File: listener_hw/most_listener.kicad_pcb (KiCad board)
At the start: 2 copper layers, 130 x 90 mm, 125 parts, among them J1 1-1394640-1, J2 ANALYSER, J3 I2S, J4 VBAT_IN, J5 PLR135/T10, J6 PLT133/T10W, J7 RCA 75R, M1 Tang Nano 20K, M2 ESP32-DevKitC-VIE, U1 74LVC1G34, U10 TPS2553DBVR, U11 74LVC1G123, U12 DIR9001, U13 SRC4192, U14 LP5907MFX-3.3, U2 74LVC1G157, U3 74LVC1G125, U4 74LVC1G123, U5 TPS7B8133DRV, U6 LMR38020F, U7 Si514, U8 LP5907MFX-3.3, U9 74LVC1G79, X1 24.576MHz

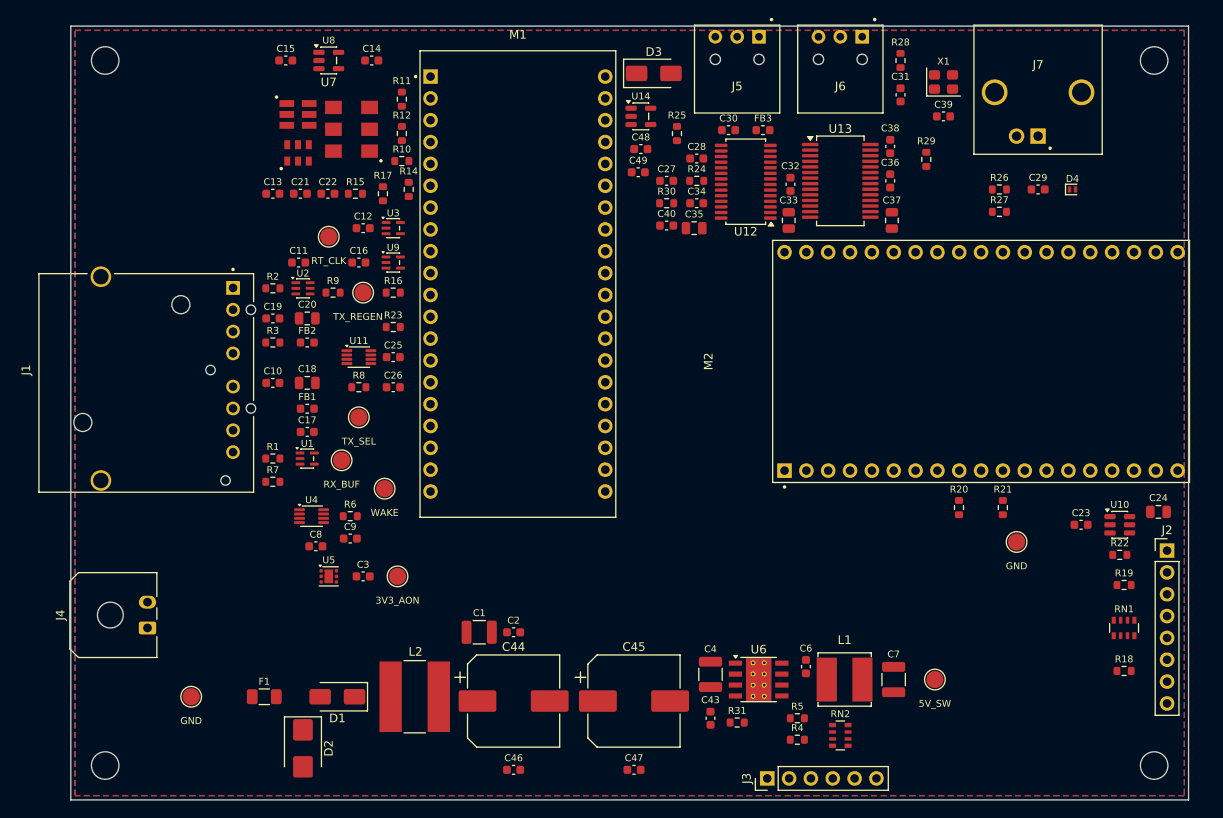
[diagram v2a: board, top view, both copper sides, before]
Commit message: Board: block 11, analog line out - PCM5102A on J3's stereo into the two RCA jacks placed by hand; footprints linked to the sheet
Sheet, block 11: U15 PCM5102A in hardware mode (FMT, FLT, DEMP low: I2S,
normal latency, no de-emphasis), SCK grounded so its PLL takes the clock from
BCK - three wires, the same I2S_BCLK_F / I2S_LRCK_F / I2S_DOUT_F that feed
J3 (64 Fs, 32-bit slots). XSMT from LOCK: muted while the ring is not locked
and while the FPGA is unconfigured (R8 holds LOCK low), with the chip's
104-sample soft ramp; no new FPGA pin, no gateware change. Outputs 2.1 Vrms
ground-centred through 470R + 2n2 C0G (TI SLAS859C Figure 33) to J8 (L) and
J9 (R), a PESD5V0S1BL at each jack as D4 at J7. U16, an LP5907, makes
3V3_DAC from 5V_SW; its output capacitance must stay within 10 uF (LP5907
data sheet), so AVDD gets 4.7 uF and CPVDD 2.2 uF instead of Figure 33's
10 uF each; LDOO 100n + 10u, flying cap and VNEG 2u2 each. Test points are
out of the BOM now (their footprints already said so). ERC clean.

Board: the placement the user reworked by hand since cddadba (the power
corner, block 9, J2/J3/U10 moved to the bottom middle, a fifth mounting hole
H5 at the top, two RCA jacks on the right edge copied from J7). The copies
became J9 (upper, right channel) and J8 (lower, left); block 11 sits in the
corner beside them, U15 turned so its analog pins face the jacks and its
digital pins face the I2S coming down from M2's pins. Every footprint now
carries its symbol's path and library name and single pins their
unconnected nets, the holes are board-only - DRC with --schematic-parity
finds no difference, so Update PCB from Schematic works from here. The
antenna keep-out is squared with M2 again. DRC: no error; the warnings are
silk, most of it in the hand-moved areas.

gen_listener_pcb.py writes the same links and parks parts its table does
not know beside the board instead of stopping. check_all.py's board step
also fails on any difference from the sheet. KiCad's local histor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
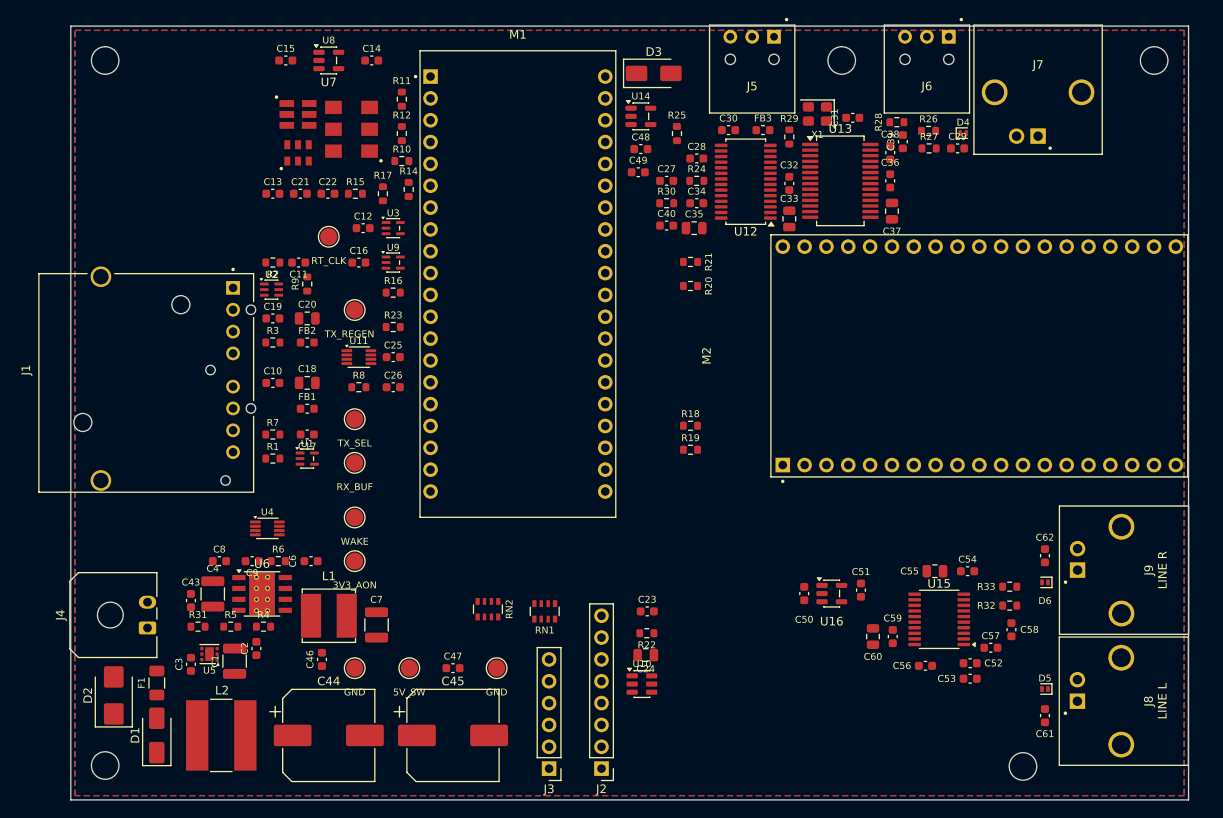
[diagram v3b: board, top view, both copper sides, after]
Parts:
- added C50: 1u, Capacitor_SMD:C_0603_1608Metric, F.Cu at (85.3, 66.0)
- added C51: 1u, Capacitor_SMD:C_0603_1608Metric, F.Cu at (91.9, 65.6)
- added C52: 100n, Capacitor_SMD:C_0603_1608Metric, F.Cu at (104.6, 74.1)
- added C53: 2u2, Capacitor_SMD:C_0603_1608Metric, F.Cu at (104.6, 75.9)
- added C54: 100n, Capacitor_SMD:C_0603_1608Metric, F.Cu at (104.3, 63.4)
- added C55: 4u7, Capacitor_SMD:C_0805_2012Metric, F.Cu at (100.5, 63.4)
- added C56: 100n, Capacitor_SMD:C_0603_1608Metric, F.Cu at (99.4, 74.4)
- added C57: 2u2, Capacitor_SMD:C_0603_1608Metric, F.Cu at (107.0, 72.3)
- added C58: 2u2, Capacitor_SMD:C_0603_1608Metric, F.Cu at (109.4, 70.2)
- added C59: 100n, Capacitor_SMD:C_0603_1608Metric, F.Cu at (95.6, 71.0)
- added C60: 10u, Capacitor_SMD:C_0805_2012Metric, F.Cu at (93.3, 71.0)
- added C61: 2n2, Capacitor_SMD:C_0603_1608Metric, F.Cu at (113.3, 80.2)
- added C62: 2n2, Capacitor_SMD:C_0603_1608Metric, F.Cu at (113.3, 61.6)
- added D5: PESD5V0S1BL, Diode_SMD:D_SOD-882, F.Cu at (113.3, 77.1)
- added D6: PESD5V0S1BL, Diode_SMD:D_SOD-882, F.Cu at (113.3, 64.7)
- added H5: M3, MountingHole_3.2mm_M3, F.Cu at (89.7, 4.00)
- added J8: LINE L, most_listener:BKL_0101153_RCA_RA, F.Cu at (117.1, 78.5)
- added J9: LINE R, most_listener:BKL_0101153_RCA_RA, F.Cu at (117.1, 63.3)
- added R32: 470, Resistor_SMD:R_0603_1608Metric, F.Cu at (109.2, 67.4)
- added R33: 470, Resistor_SMD:R_0603_1608Metric, F.Cu at (109.2, 65.2)
- added U15: PCM5102A, Package_SO:TSSOP-20_4.4x6.5mm_P0.65mm, F.Cu at (101.0, 69.0)
- added U16: LP5907MFX-3.3, Package_TO_SOT_SMD:SOT-23-5, F.Cu at (88.5, 66.0)
- C1, C4, C7: footprint C_1210_3225Metric -> Capacitor_SMD:C_1210_3225Metric
- C10, C11, C12, C13, C14, C15, C16, C17, C19, C2, C21, C22, C23, C25, C26, C27, C28, C29, C3, C30, C31, C32, C34, C36, C38, C39, C40, C43, C46, C47, C48, C49, C6, C8, C9: footprint C_0603_1608Metric -> Capacitor_SMD:C_0603_1608Metric
- C18, C20, C24, C33, C35, C37: footprint C_0805_2012Metric -> Capacitor_SMD:C_0805_2012Metric
- C44, C45: footprint CP_Elec_10x10.5 -> Capacitor_SMD:CP_Elec_10x10.5
- D1, D3: footprint D_SMA -> Diode_SMD:D_SMA
- D2: footprint D_SMB -> Diode_SMD:D_SMB
- D4: footprint D_SOD-882 -> Diode_SMD:D_SOD-882
- F1: footprint Fuse_1206_3216Metric -> Fuse:Fuse_1206_3216Metric
- FB1, FB2, FB3: footprint L_0603_1608Metric -> Inductor_SMD:L_0603_1608Metric
- J1: footprint TE_MOST_Pigtail_FOT_2+0 -> most_listener:TE_MOST_Pigtail_FOT_2+0
- J2: footprint PinHeader_1x08_P2.54mm_Vertical -> Connector_PinHeader_2.54mm:PinHeader_1x08_P2.54mm_Vertical
- J3: footprint PinHeader_1x06_P2.54mm_Vertical -> Connector_PinHeader_2.54mm:PinHeader_1x06_P2.54mm_Vertical
- J4: footprint Molex_Micro-Fit_3.0_43650-0200_1x02_P3.00mm_Horizontal -> Connector_Molex:Molex_Micro-Fit_3.0_43650-0200_1x02_P3.00mm_Horizontal
- J5, J6: footprint Everlight_TOSLINK_T10 -> most_listener:Everlight_TOSLINK_T10
- J7: footprint BKL_0101153_RCA_RA -> most_listener:BKL_0101153_RCA_RA
- L1: footprint L_Bourns_SRN6045TA -> Inductor_SMD:L_Bourns_SRN6045TA
- L2: footprint L_Bourns-SRN8040_8x8.15mm -> Inductor_SMD:L_Bourns-SRN8040_8x8.15mm
- M1: footprint Sipeed_TangNano20K -> most_listener:Sipeed_TangNano20K
- M2: footprint Espressif_ESP32-DevKitC_V4 -> most_listener:Espressif_ESP32-DevKitC_V4
- R1, R10, R11, R12, R14, R15, R16, R17, R18, R19, R2, R20, R21, R22, R23, R24, R25, R26, R27, R28, R29, R3, R30, R31, R4, R5, R6, R7, R8, R9: footprint R_0603_1608Metric -> Resistor_SMD:R_0603_1608Metric
- RN1, RN2: footprint R_Array_Convex_4x0603 -> Resistor_SMD:R_Array_Convex_4x0603
- TP1, TP2, TP3, TP4, TP5, TP6, TP7, TP8, TP9: footprint TestPoint_Pad_D2.0mm -> TestPoint:TestPoint_Pad_D2.0mm
- U1, U3, U9: footprint SOT-353_SC-70-5 -> Package_TO_SOT_SMD:SOT-353_SC-70-5
- U10: footprint SOT-23-6 -> Package_TO_SOT_SMD:SOT-23-6
- U11, U4: footprint VSSOP-8_2.3x2mm_P0.5mm -> Package_SO:VSSOP-8_2.3x2mm_P0.5mm
- U12: footprint TSSOP-28_4.4x9.7mm_P0.65mm -> Package_SO:TSSOP-28_4.4x9.7mm_P0.65mm
- U13: footprint SSOP-28_5.3x10.2mm_P0.65mm -> Package_SO:SSOP-28_5.3x10.2mm_P0.65mm
- U14, U8: footprint SOT-23-5 -> Package_TO_SOT_SMD:SOT-23-5
- U2: footprint SOT-363_SC-70-6 -> Package_TO_SOT_SMD:SOT-363_SC-70-6
- U5: footprint WSON-6-1EP_2x2mm_P0.65mm_EP1x1.6mm -> Package_SON:WSON-6-1EP_2x2mm_P0.65mm_EP1x1.6mm
- U6: footprint Texas_HSOP-8-1EP_3.9x4.9mm_P1.27mm_ThermalVias -> Package_SO:Texas_HSOP-8-1EP_3.9x4.9mm_P1.27mm_ThermalVias
- U7: footprint Si514_5x7_3.2x5_2.5x3.2 -> most_listener:Si514_5x7_3.2x5_2.5x3.2
- X1: footprint Oscillator_SMD_Abracon_ASE-4Pin_3.2x2.5mm -> Oscillator:Oscillator_SMD_Abracon_ASE-4Pin_3.2x2.5mm
- moved J2 70.5 mm to (61.7, 86.4), turned to 180 degrees
- moved RN1 67.4 mm to (55.1, 68.1), turned to -90 degrees
- moved R5 66.8 mm to (18.6, 69.8)
- moved R31 63.7 mm to (14.8, 69.8)
- moved R4 63.5 mm to (22.4, 69.8)
- moved TP9 62.2 mm to (49.5, 74.7)
- moved C43 62.0 mm to (14.0, 66.8)
- moved C24 61.9 mm to (66.9, 73.2), turned to 180 degrees
- moved TP7 61.1 mm to (39.4, 74.7)
- moved C7 60.5 mm to (35.6, 69.6)
- moved L1 60.4 mm to (30.0, 68.6)
- moved C6 58.9 mm to (27.9, 62.2), turned to 180 degrees
- moved C4 58.6 mm to (16.5, 66.0)
- moved U6 58.6 mm to (22.2, 66.0)
- moved U10 58.6 mm to (66.4, 76.5)
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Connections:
- J1 pad 7: (no net) -> unconnected-(J1-STATUS-Pad7)
- M1 pad 11: (no net) -> unconnected-(M1-26_LCD_VS-Pad11)
- M1 pad 15: (no net) -> unconnected-(M1-17_LED2-Pad15)
- M1 pad 16: (no net) -> unconnected-(M1-20_LED5-Pad16)
- M1 pad 17: (no net) -> unconnected-(M1-19_LED4-Pad17)
- M1 pad 18: (no net) -> unconnected-(M1-18_LED3-Pad18)
- M1 pad 27: (no net) -> unconnected-(M1-56_I2S_BCLK-Pad27)
- M1 pad 29: (no net) -> unconnected-(M1-51_PA_EN-Pad29)
- M1 pad 31: (no net) -> unconnected-(M1-55_I2S_LRCK-Pad31)
- M1 pad 34: (no net) -> unconnected-(M1-79_WS2812-Pad34)
- M1 pad 36: (no net) -> unconnected-(M1-3V3-Pad36)
- M1 pad 39: (no net) -> unconnected-(M1-53_EDID_CLK-Pad39)
- M1 pad 40: (no net) -> unconnected-(M1-52_EDID_DAT-Pad40)
- M1 pad 6: (no net) -> unconnected-(M1-15_LED0-Pad6)
- M1 pad 7: (no net) -> unconnected-(M1-16_LED1-Pad7)
- M2 pad 1: (no net) -> unconnected-(M2-3V3-Pad1)
- M2 pad 10: (no net) -> unconnected-(M2-IO26-Pad10)
- M2 pad 12: (no net) -> unconnected-(M2-IO14-Pad12)
- M2 pad 13: (no net) -> unconnected-(M2-IO12-Pad13)
- M2 pad 15: (no net) -> unconnected-(M2-IO13-Pad15)
- M2 pad 16: (no net) -> unconnected-(M2-D2-Pad16)
- M2 pad 17: (no net) -> unconnected-(M2-D3-Pad17)
- M2 pad 18: (no net) -> unconnected-(M2-CMD-Pad18)
- M2 pad 2: (no net) -> unconnected-(M2-EN-Pad2)
- M2 pad 21: (no net) -> unconnected-(M2-IO23-Pad21)
- M2 pad 22: (no net) -> unconnected-(M2-IO22-Pad22)
- M2 pad 23: (no net) -> unconnected-(M2-TX-Pad23)
- M2 pad 24: (no net) -> unconnected-(M2-RX-Pad24)
- M2 pad 25: (no net) -> unconnected-(M2-IO21-Pad25)
- M2 pad 27: (no net) -> unconnected-(M2-IO19-Pad27)
- M2 pad 28: (no net) -> unconnected-(M2-IO18-Pad28)
- M2 pad 29: (no net) -> unconnected-(M2-IO5-Pad29)
- M2 pad 3: (no net) -> unconnected-(M2-VP-Pad3)
- M2 pad 30: (no net) -> unconnected-(M2-IO17-Pad30)
- M2 pad 31: (no net) -> unconnected-(M2-IO16-Pad31)
- M2 pad 32: (no net) -> unconnected-(M2-IO4-Pad32)
- M2 pad 33: (no net) -> unconnected-(M2-IO0-Pad33)
- M2 pad 34: (no net) -> unconnected-(M2-IO2-Pad34)
- M2 pad 35: (no net) -> unconnected-(M2-IO15-Pad35)
- M2 pad 36: (no net) -> unconnected-(M2-D1-Pad36)
- M2 pad 37: (no net) -> unconnected-(M2-D0-Pad37)
- M2 pad 38: (no net) -> unconnected-(M2-CLK-Pad38)
- M2 pad 4: (no net) -> unconnected-(M2-VN-Pad4)
- U1 pad 1: (no net) -> unconnected-(U1-NC-Pad1)
- U10 pad 4: (no net) -> unconnected-(U10-~{FAULT}-Pad4)
- U12 pad 1: (no net) -> unconnected-(U12-AUDIO-Pad1)
- U12 pad 15: (no net) -> unconnected-(U12-COUT-Pad15)
- U12 pad 16: (no net) -> unconnected-(U12-UOUT-Pad16)
- U12 pad 17: (no net) -> unconnected-(U12-EMPH-Pad17)
- U12 pad 18: (no net) -> unconnected-(U12-BFRAME-Pad18)
- U12 pad 2: (no net) -> unconnected-(U12-FSOUT0-Pad2)
- U12 pad 3: (no net) -> unconnected-(U12-FSOUT1-Pad3)
- U12 pad 4: (no net) -> unconnected-(U12-SCKO-Pad4)
- U12 pad 7: (no net) -> unconnected-(U12-XTO-Pad7)
- U12 pad 9: (no net) -> unconnected-(U12-CLKST-Pad9)
- U13 pad 15: (no net) -> unconnected-(U13-RDY-Pad15)
- U13 pad 3: (no net) -> unconnected-(U13-NC-Pad3)
- U14 pad 4: (no net) -> unconnected-(U14-NC-Pad4)
- U5 pad 5: (no net) -> unconnected-(U5-NC-Pad5)
- U6 pad 6: (no net) -> unconnected-(U6-PG-Pad6)
- U7 pad 5: (no net) -> unconnected-(U7-CLK--Pad5)
- U8 pad 4: (no net) -> unconnected-(U8-NC-Pad4)

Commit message: Board: the user's regroup, reviewed - 33R singles under M1 at their FPGA pins, U14 back in block 9, block 9 turned to its jacks, the capacitor copies out
The user regrouped the board: M2 upright against M1 with both USB ends at
the top edge, every audio jack (TOSLINK in and out, coax, the two line-out
RCA) on the right edge, block 9 beside them, the host switch and the test
points in the bottom middle, a sixth mounting hole (H6) on the left edge.
Agreed after review and done here:

- Sheet: RN1 and RN2 (4 x 33R arrays) became single 0603 resistors, R34..R41,
  so each FPGA output to J2/J3 has its own. With R18..R21 they sit under M1,
  each beside its FPGA pin (source termination: MCLK, BCLK and TDM lines run
  to the headers and on through cables). The Tang Nano's footprint now keeps
  only its two socket rows as courtyard, so low parts may sit under the
  module standing on its 8.5 mm sockets; its outline stays on fab and silk.
  R20 had landed on M2's pins 37/38 (the seven DRC errors of the regroup);
  it sits at M1 pin 1 now. ERC clean.
- U14 with C48/C49 back in block 9: the clean 3V3_DA stays short, the long
  run is 5V_SW's.
- Block 9 re-laid for the jacks on the right edge: DIR9001 next to J5 with
  RXIN and its loop filter towards the jack, SRC4192 between it and the
  modules with its I2S outputs towards them, X1 at RCKI, FB3/C30 within 2 cm
  of J5 as the Everlight sheet asks, C31 by J6, the coax divider and D4 by J7.
- The three board-only copies each of C45 and C47 are gone: two 100 uF
  pairs are what the input needs; more only raises the inrush through F1.
- Both antenna keep-outs squared with M2 upright (the B.Cu one was half
  height); C61/D5 and C62/D6 moved up with J8/J9.

DRC: no error; 368 unconnected (not routed); the warnings are silk, for the
final silk pass. DRC with --schematic-parity: no difference. The board
generator's table lost RN1/RN2; a fresh layout parks the parts it does not
know beside the board and still matches the sheet.

Co-Au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
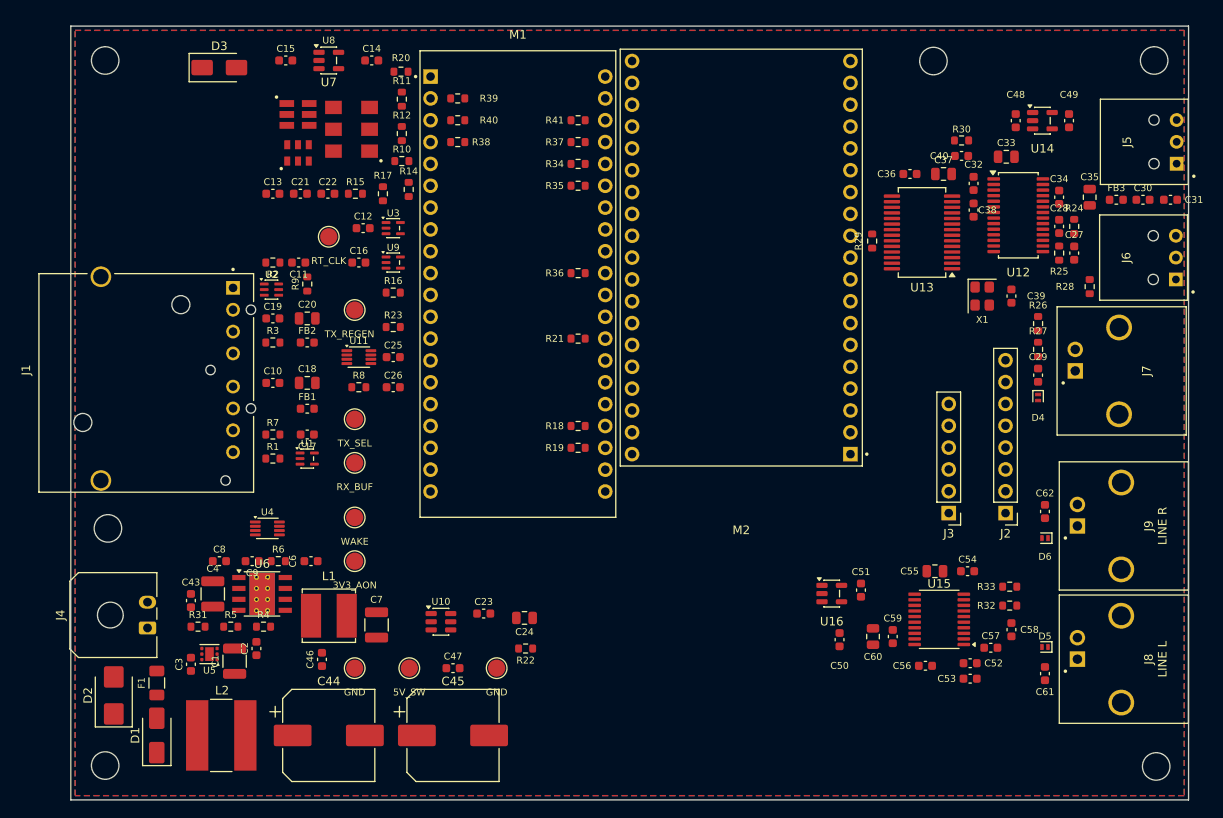
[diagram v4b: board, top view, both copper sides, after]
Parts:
- removed RN1, RN2: 4x33, Resistor_SMD:R_Array_Convex_4x0603
- added H6: M3, MountingHole_3.2mm_M3, F.Cu at (4.32, 58.4)
- added R34: 33, Resistor_SMD:R_0603_1608Metric, F.Cu at (59.0, 16.0)
- added R35: 33, Resistor_SMD:R_0603_1608Metric, F.Cu at (59.0, 18.6)
- added R36: 33, Resistor_SMD:R_0603_1608Metric, F.Cu at (59.0, 28.7)
- added R37: 33, Resistor_SMD:R_0603_1608Metric, F.Cu at (59.0, 13.5)
- added R38: 33, Resistor_SMD:R_0603_1608Metric, F.Cu at (45.0, 13.5)
- added R39: 33, Resistor_SMD:R_0603_1608Metric, F.Cu at (45.0, 8.41)
- added R40: 33, Resistor_SMD:R_0603_1608Metric, F.Cu at (45.0, 10.9)
- added R41: 33, Resistor_SMD:R_0603_1608Metric, F.Cu at (59.0, 10.9)
- moved J2 55.6 mm to (108.7, 56.6)
- moved J3 55.2 mm to (102.1, 56.6)
- moved J5 50.9 mm to (128.6, 13.5), turned to 90 degrees
- moved D3 50.5 mm to (17.3, 4.83)
- moved C49 50.5 mm to (116.1, 11.0), turned to -90 degrees
- moved C30 48.9 mm to (124.7, 20.2), turned to 180 degrees
- moved C27 48.1 mm to (116.7, 26.4), turned to 90 degrees
- moved U14 46.7 mm to (113.0, 11.0)
- moved R25 46.6 mm to (115.0, 26.4)
- moved C35 46.1 mm to (118.5, 19.9), turned to -90 degrees
- moved R24 44.2 mm to (116.7, 23.3), turned to 90 degrees
- moved C48 43.7 mm to (109.9, 11.0), turned to 90 degrees
- moved C28 42.9 mm to (115.0, 23.3), turned to -90 degrees
- moved C34 42.2 mm to (115.0, 19.9), turned to -90 degrees
- moved R20 41.9 mm to (38.4, 5.30), turned to 180 degrees
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
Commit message: Board: M1 and M2 left into the strip the user freed; resistors of M1's pins under it; signal test points above J1
The user cleared a vertical strip left of M1 and asked for the FPGA to move
into it, part of the resistors to go under the module, and the signal test
points to go to the left edge above the MOST header.

- The ring-logic column (U3, U9, R16) with R17 moved into the strip; M1
  followed it 6.7 mm to the left and M2 with M1, the two modules still side
  by side; the antenna keep-out moved with M2. The free space now lies
  between M2 and block 9, a channel for M2's signals to the right half.
- Under M1, each beside its pin, as before for J2/J3's 33R: R20 (pin 1,
  UART_RX_F), R14 (pin 5, CLK_1024's pull-down), R11/R12 (pins 12/13, the
  Si514 I2C pull-ups). R10, the 22R source termination of the Si514's
  output, went to the Si514 next to R15, not to the FPGA end.
- Parts left behind by the regroup rejoined their chips: U11's timing RC
  (R23, C25) and decoupling (C26) at U11, C14 at U8's output.
- The signal test points RX_BUF, TX_REGEN, TX_SEL, WAKE, RT_CLK sit in a
  block above J1 with two ground points beside them: TP8 and TP10, the copy
  of TP8 the user had made, now its own part in the sheet (block 10). TP7
  (5V_SW) came out from under M1's HDMI connector.

ERC clean; DRC: no error, no difference from the sheet; the warnings are
silk, for the final silk pass. The board generator tolerates test points
its table does not know (TP10).

Co-Authored-By: Claude Opus 5.5 <noreply@anthropic.com>
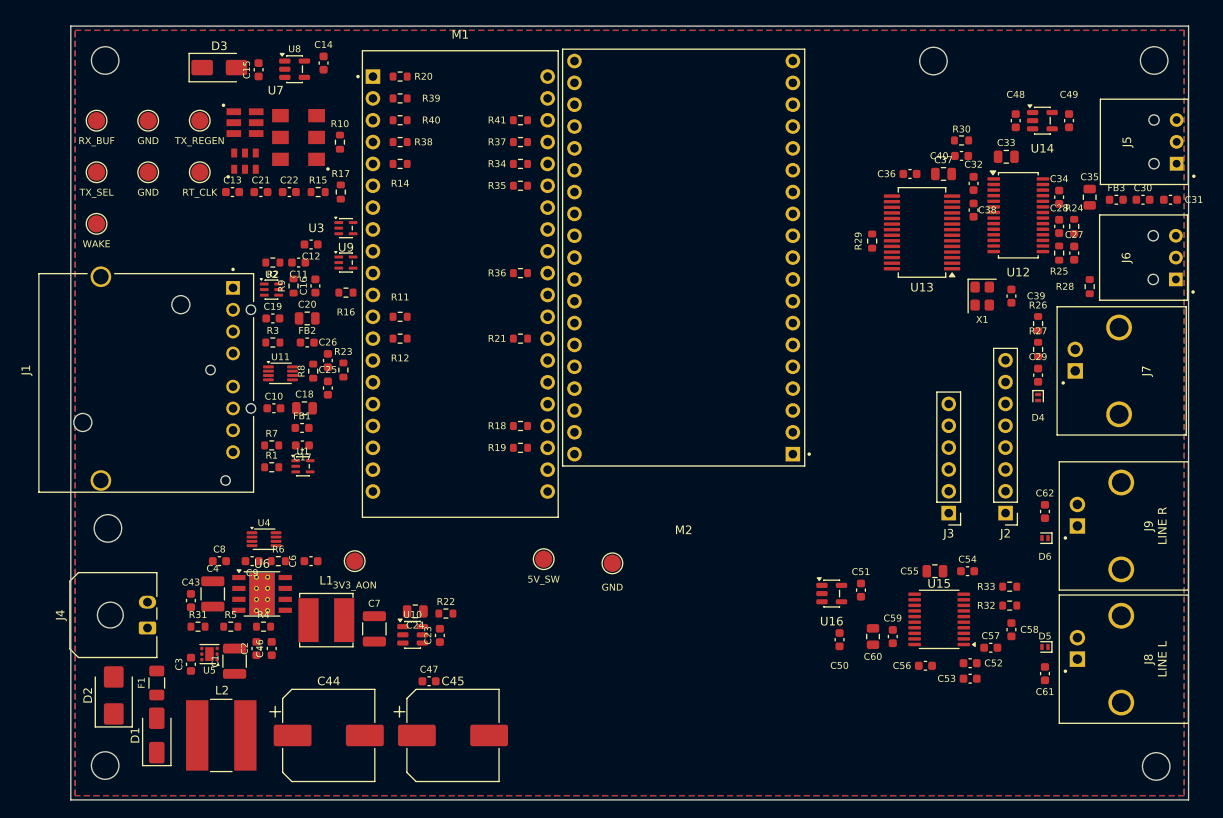
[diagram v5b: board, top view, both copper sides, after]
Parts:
- added TP8: GND, TestPoint:TestPoint_Pad_D2.0mm, F.Cu at (9.00, 11.0)
- moved TP10 62.5 mm to (9.00, 17.0)
- moved TP1 49.9 mm to (3.00, 11.0)
- moved TP4 45.5 mm to (3.00, 23.0)
- moved TP3 41.5 mm to (3.00, 17.0)
- moved TP2 28.5 mm to (15.0, 11.0)
- moved R11 25.3 mm to (38.3, 33.8), turned to 0 degrees
- moved R12 23.9 mm to (38.3, 36.4), turned to 0 degrees
- moved TP7 20.1 mm to (55.0, 62.0)
- moved TP9 18.2 mm to (63.0, 62.5)
- moved TP5 16.8 mm to (15.0, 17.0)
- moved C24 12.7 mm to (40.1, 68.1)
- moved R22 10.1 mm to (43.6, 68.3), turned to 0 degrees
- moved U11 9.31 mm to (24.4, 40.4)
- moved C25 8.41 mm to (29.9, 42.1), turned to -90 degrees
- moved C26 8.21 mm to (29.9, 38.9), turned to 90 degrees
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- renumbered TP8 to TP10
